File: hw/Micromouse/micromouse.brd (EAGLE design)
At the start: 160 x 100 mm, 23 parts, among them IC1 DSPIC33FJ64MC804-PT, IC2 DRV8833PWR, IC3 LM1117IDTX-5.0_NOPB, IC4 LM1117IDTX-3.3_NOPB, Y1 ECS-200-18-4X-CKM

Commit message: Updated schematic
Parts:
- removed HDR3, HDR4: (no value), SparkFun-Connectors:1X11
- removed IC3: LM1117IDTX-5.0_NOPB, SamacSys_Parts:LM1117IDTX50NOPB
- removed IC4: LM1117IDTX-3.3_NOPB, SamacSys_Parts:LM1117IDTX33NOPB
- removed MOTOR1, MOTOR2: (no value), con-harting:CON06
- removed SENSOR1, SENSOR2, SENSOR3: B3B-ZR(LF)(SN), Headers:B3B-ZR(LF)(SN)
- added C10: 10u, micromouse:0805_POL
- added C11, C12: 100n, micromouse:0805
- added C8: 0.01u, micromouse:0805
- added C9: 2u2, micromouse:0805
- added LED2, LED3, LED4, LED5: (no value), micromouse:LED_3MM
- added M1, M2: (no value), micromouse:JP3Q
- added R1: 0.2, micromouse:0805
- added R10, R2, R4: 10k, micromouse:0805
- added R11, R3, R5: 1k, micromouse:0805
- added R6, R7, R8, R9: 130, micromouse:0805
- added REG1: LM1117-5.0V, micromouse:SOT-223-4
- added REG2: LM1117-3.3V, micromouse:SOT-223-4
- added S1, S3: GP2Y0A51SK0F, micromouse:JP2Y
- added S2: GP2Y0A41SK0F, micromouse:JP2Y
- added SW1, SW2, SW3: B3F-1000, micromouse:B3F-1000
- added T1, T2, T3, T4: NHDTC1X4ETR, micromouse:SOT23
- C1, C2, C3, C4, C5: device micromouse:C0805 -> micromouse:0805_POL
- C6, C7: value C0805C220F5GACTU -> 15p; device SamacSys_Parts:CAPC2012X90N -> micromouse:0805
- HDR1: value (none) -> PICKIT_CON; device SparkFun-Connectors:1X11 -> micromouse:6PIN
- HDR2: value (none) -> UART_CON; device SparkFun-Connectors:1X11 -> micromouse:JP2Y
- Y1: value ECS-200-18-4X-CKM -> (none); device ECS-200-18-4X-CKM:XTAL_ECS-200-18-4X-CKM -> SparkFun-Clocks:HC49US
- moved C7 41.5 mm to (118.1, 55.9)
- moved IC1 36.0 mm to (73.7, 71.1)
- moved C1 35.4 mm to (57.1, 58.4)
- moved HDR1 33.3 mm to (73.7, 31.8)
- moved HDR2 32.1 mm to (45.7, 40.6)
- moved C6 31.0 mm to (111.8, 57.1)
- moved C3 29.8 mm to (90.2, 50.8), turned to 0 degrees
- moved Y1 27.9 mm to (113.0, 48.3), turned to 90 degrees
- moved C2 22.9 mm to (69.8, 36.8)
- moved G1 20.5 mm to (99.1, 49.5)
- moved C4 19.4 mm to (90.2, 44.5), turned to 0 degrees
- moved C5 15.3 mm to (90.2, 39.4), turned to 0 degrees
- moved IC2 1.27 mm to (128.3, 57.1)
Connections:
- net N$1 renamed OSC2
- net N$2 renamed OSC1
- removed net VDD1: IC1.40
- removed net VSS2: IC1.39
- new net LED1: T1.1
- new net LED2: T2.1
- new net LED3: T3.1
- new net LED4: T4.1
- new net M1+: IC2.2, M1.2
- new net M1-: IC2.4, M1.1
- new net M1_CHA: M1.5
- new net M1_CHB: M1.6
- new net M1_IN1: IC2.16
- new net M1_IN2: IC2.15
- new net M2+: IC2.7, M2.2
- new net M2-: IC2.5, M2.1
- new net M2_CHA: M2.5
- new net M2_CHB: M2.6
- new net M2_IN1: IC2.9
- new net M2_IN2: IC2.10
- new net N$10: R7.2, T2.3
- new net N$11: LED3.K, R7.1
- new net N$12: R8.2, T3.3
- new net N$13: LED4.K, R8.1
- new net N$14: R9.2, T4.3
- new net N$15: LED5.K, R9.1
- new net N$16: C11.1, R10.2, R11.1, SW3.4
- new net N$3: C8.2, IC2.11
- new net N$4: C9.1, IC2.14
- new net N$5: IC2.3, IC2.6, R1.1
- new net N$6: C12.1, R4.2, R5.1, SW2.4
- new net N$7: R2.2, R3.1, SW1.4
- new net N$8: R6.2, T1.3
- new net N$9: LED2.K, R6.1
- new net PGC: HDR1.4
- new net PGD: HDR1.5
- new net S1_OUT: S1.1
- new net S2_OUT: S2.3
- new net S3_OUT: S3.1
- new net SW1: R5.2
- new net SW2: R11.2
- new net UART_RX: HDR2.2
- new net UART_TX: HDR2.1
- net +3V3: now also HDR1.2, IC1.40, IC2.1, IC2.8, M1.4, M2.4, R10.1, R2.1, R4.1, REG2.2, REG2.4; no longer IC4.2
- net +5V: now also LED2.A, LED3.A, LED4.A, LED5.A, REG1.2, REG1.4, REG2.3, S1.3, S2.1, S3.3; no longer IC3.4, IC4.3
- net +9V: now also C10.1, C8.1, IC2.12, REG1.3; no longer IC3.3
- net GND: now also C10.2, C11.2, C12.2, C9.2, HDR1.3, HDR2.3, IC1.39, M1.3, M2.3, R1.2, REG1.1, REG2.1, S1.2, S2.2, S3.2, SW1.2, SW2.2, SW3.2, T1.2, T2.2, T3.2, T4.2; no longer IC3.1, IC4.1
- net MCLR: now also HDR1.1, R3.2

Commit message: Updated EAGLE project
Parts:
- removed S1, S3: GP2Y0A51SK0F, micromouse:JP2Y
- removed S2: GP2Y0A41SK0F, micromouse:JP2Y
- added J1, J2: GP2Y0A51SK0F, micromouse:B3B-ZR(LF)(SN)
- added J3: GP2Y0A41SK0F, micromouse:B3B-PH-K-S
- added R12: 0.2, micromouse:0805
- moved C8 152.7 mm to (-4.45, -1.27)
- moved C9 150.4 mm to (-0.64, -1.91), turned to 270 degrees
- moved C10 144.2 mm to (-7.62, -1.27), turned to 90 degrees
- moved IC2 141.5 mm to (-3.81, 6.35), turned to 270 degrees
- moved R1 134.3 mm to (0.64, 8.89), turned to 270 degrees
- moved C6 127.7 mm to (-11.5, 23.6), turned to 180 degrees
- moved M2 126.5 mm to (-21.6, 17.1)
- moved C7 126.1 mm to (-3.76, 23.6)
- moved M1 123.2 mm to (-5.71, 17.1)
- moved Y1 122.5 mm to (-7.62, 27.3), turned to 180 degrees
- moved HDR1 108.7 mm to (-3.81, -44.5)
- moved HDR2 91.1 mm to (0.00, -38.1), turned to 180 degrees
- moved IC1 88.6 mm to (-8.26, 37.5), turned to 270 degrees
- moved C3 87.3 mm to (3.17, 43.8), turned to 180 degrees
- moved R7 82.8 mm to (-22.9, 37.5), turned to 90 degrees
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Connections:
- new net N$1: IC2.6, R12.1
- net +5V: now also J1.1, J2.1, J3.3; no longer S1.3, S2.1, S3.3
- net GND: now also J1.2, J2.2, J3.2, R12.2; no longer S1.2, S2.2, S3.2
- net N$5: no longer IC2.6
- net S1_OUT: now also J1.3; no longer S1.1
- net S2_OUT: now also J3.1; no longer S2.3
- net S3_OUT: now also J2.3; no longer S3.1
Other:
- board size 160 x 100 mm -> 60 x 112 mm

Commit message: First routing on PCB
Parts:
- removed R10: 10k, micromouse:0805
- removed R11: 1k, micromouse:0805
- removed SW2, SW3: B3F-1000, micromouse:B3F-1000
- added C13, C14: (no value), micromouse:0805
- added SW_RST: B3F-1000, micromouse:B3F-1000
- C11: value 100n -> (none)
- moved HDR1 82.8 mm to (-27.9, 34.8), turned to 270 degrees
- moved HDR2 80.7 mm to (12.0, 41.7)
- moved R4 68.7 mm to (-0.11, -37.1)
- moved SW1 66.0 mm to (0.09, -29.4), turned to 0 degrees
- moved R5 63.6 mm to (3.23, -35.3), turned to 270 degrees
- moved C12 61.0 mm to (-0.12, -34.2), turned to 180 degrees
- moved LED3 49.1 mm to (-4.10, -5.82)
- moved R7 49.1 mm to (0.34, -5.82)
- moved T2 49.1 mm to (3.52, -5.82)
- moved LED2 49.1 mm to (-4.10, 0.53)
- moved LED4 49.1 mm to (-4.10, -12.2)
- moved LED5 49.1 mm to (-4.10, -18.5)
- moved R6 49.1 mm to (0.34, 0.53)
- moved R8 49.1 mm to (0.34, -12.2)
- moved R9 49.1 mm to (0.34, -18.5)
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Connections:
- removed net N$16: C11.1, R10.2, R11.1, SW3.4
- removed net PGC: HDR1.4
- removed net PGD: HDR1.5
- removed net PGEC1: IC1.22
- removed net PGED1: IC1.21
- removed net SW2: R11.2
- net +3V3: now also C11.1, C13.2, C14.2; no longer R10.1
- net GND: now also C13.1, C14.1, SW_RST.2; no longer SW2.2, SW3.2
- net M1_CHA: now also IC1.36, M1.6; no longer M1.5
- net M1_CHB: now also IC1.37, M1.5; no longer M1.6
- net M1_IN1: now also IC1.1
- net M1_IN2: now also IC1.2
- net M2_CHA: now also IC1.43, M2.6; no longer M2.5
- net M2_CHB: now also IC1.44, M2.5; no longer M2.6
- net M2_IN1: now also IC1.4
- net M2_IN2: now also IC1.3
- net N$6: now also SW1.4; no longer SW2.4
- net N$7: now also SW_RST.4; no longer SW1.4
- net PGEC3: now also HDR1.5
- net PGED3: now also HDR1.4
- net S1_OUT: now also IC1.20
- net S2_OUT: now also IC1.21
- net S3_OUT: now also IC1.22
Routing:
- net +3V3: track 0.00 -> 158.0 mm, vias 0 -> 3
- net +5V: track 0.00 -> 79.0 mm
- net M1+: track 0.00 -> 65.5 mm, vias 0 -> 1
- net M1-: track 0.00 -> 59.6 mm, vias 0 -> 1
- net +9V: track 0.00 -> 54.1 mm
- net M2-: track 0.00 -> 41.6 mm, vias 0 -> 1
- net M2+: track 0.00 -> 39.7 mm, vias 0 -> 1
- net MCLR: track 0.00 -> 35.1 mm
- net PGEC3: track 0.00 -> 28.4 mm, vias 0 -> 1
- net PGED3: track 0.00 -> 27.3 mm, vias 0 -> 1
- net S1_OUT: track 0.00 -> 22.0 mm
- net M1_CHB: track 0.00 -> 19.8 mm
- net M1_CHA: track 0.00 -> 17.6 mm
- net S2_OUT: track 0.00 -> 16.8 mm
- net M2_CHB: track 0.00 -> 13.1 mm
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
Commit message: Cleanup on PCB routing
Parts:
- moved C2 4.40 mm to (28.3, 17.9), turned to 270 degrees
- moved G1 3.16 mm to (20.1, 14.9)
- moved REG1 3.06 mm to (25.9, 24.8)
- moved C3 2.83 mm to (22.6, 29.4)
- moved C5 2.80 mm to (25.7, 42.6)
- moved REG2 2.80 mm to (24.7, 36.9)
- moved HDR2 2.72 mm to (13.6, 39.5)
- moved C6 2.15 mm to (-18.8, 30.8), turned to 90 degrees
- moved C7 1.31 mm to (-18.8, 35.8), turned to 90 degrees
- moved C1 0.72 mm to (1.94, 36.4)
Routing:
- net +9V: track 54.1 -> 66.9 mm
- net N$7: track 0.28 -> 7.00 mm
- net +5V: track 79.0 -> 74.3 mm
- net +3V3: track 158.0 -> 161.8 mm
- net N$1: track 8.52 -> 7.70 mm
- net VCAP/VDDCORE: track 3.02 -> 2.25 mm

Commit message: Updated PCB
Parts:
- moved LED5 15.0 mm to (-5.30, -33.5)
- moved R9 15.0 mm to (-0.85, -33.5)
- moved T4 15.0 mm to (2.32, -33.5)
- moved LED4 15.0 mm to (-5.30, -27.2)
- moved R8 15.0 mm to (-0.85, -27.2)
- moved T3 15.0 mm to (2.32, -27.2)
- moved LED2 15.0 mm to (-5.30, -14.5)
- moved LED3 15.0 mm to (-5.30, -20.8)
- moved R6 15.0 mm to (-0.85, -14.5)
- moved R7 15.0 mm to (-0.85, -20.8)
- moved T1 15.0 mm to (2.32, -14.5)
- moved T2 15.0 mm to (2.32, -20.8)
- moved G1 14.9 mm to (5.33, 16.9), turned to 180 degrees
- moved R5 13.9 mm to (-6.47, -45.2), turned to 180 degrees
- moved SW1 12.7 mm to (-0.64, -42.1), turned to 270 degrees
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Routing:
- net +5V: track 74.3 -> 155.6 mm, vias 0 -> 1
- net +3V3: track 161.8 -> 228.7 mm
- net M2+: track 39.7 -> 55.0 mm
- net +9V: track 66.9 -> 81.4 mm
- net GND: track 0.00 -> 9.08 mm, vias 0 -> 11
- net M2-: track 41.6 -> 49.0 mm
- net M1-: track 59.6 -> 64.7 mm
- net M1+: track 65.5 -> 70.3 mm
- net N$9: track 0.00 -> 3.57 mm
- net N$13: track 0.00 -> 3.57 mm
- net N$11: track 0.00 -> 3.57 mm
- net N$15: track 0.00 -> 3.57 mm
- net N$14: track 0.00 -> 2.47 mm
- net N$12: track 0.00 -> 2.47 mm
- net N$8: track 0.00 -> 2.47 mm
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
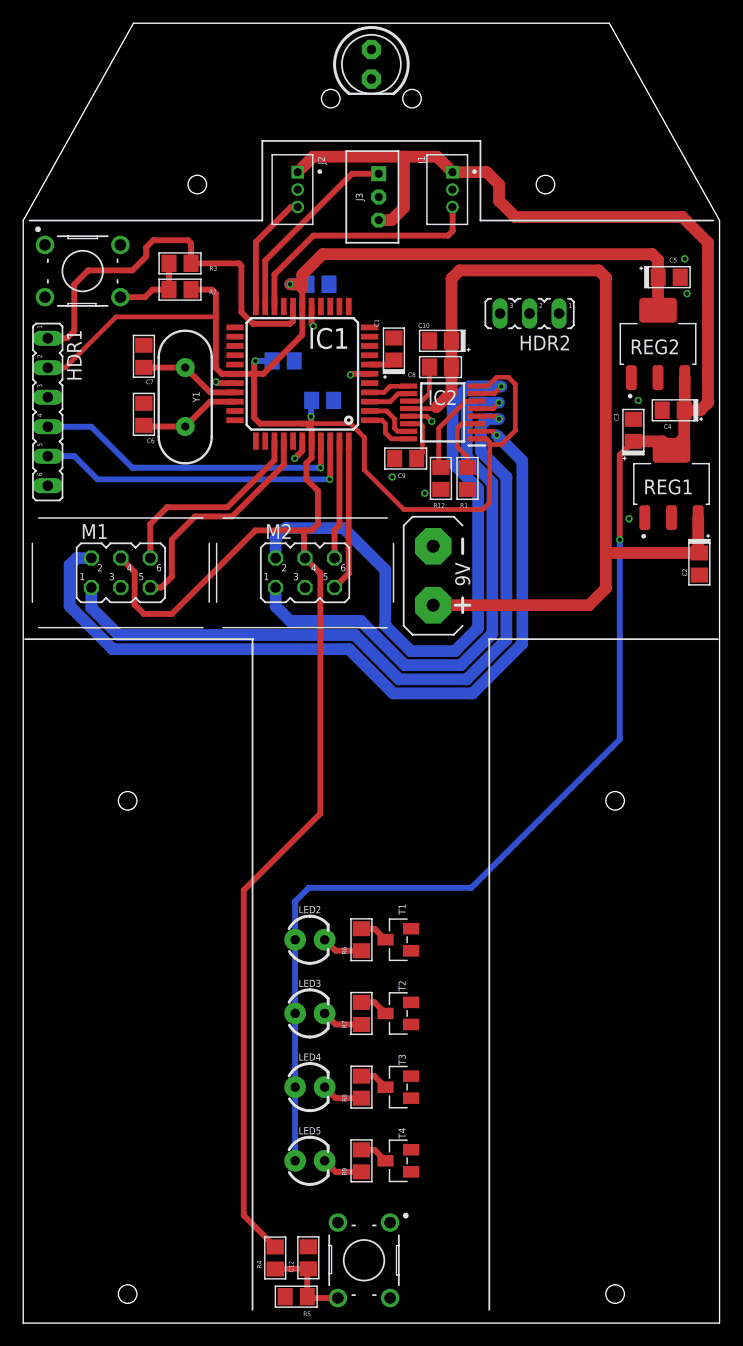
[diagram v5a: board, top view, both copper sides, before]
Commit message: Added Bluetooth module
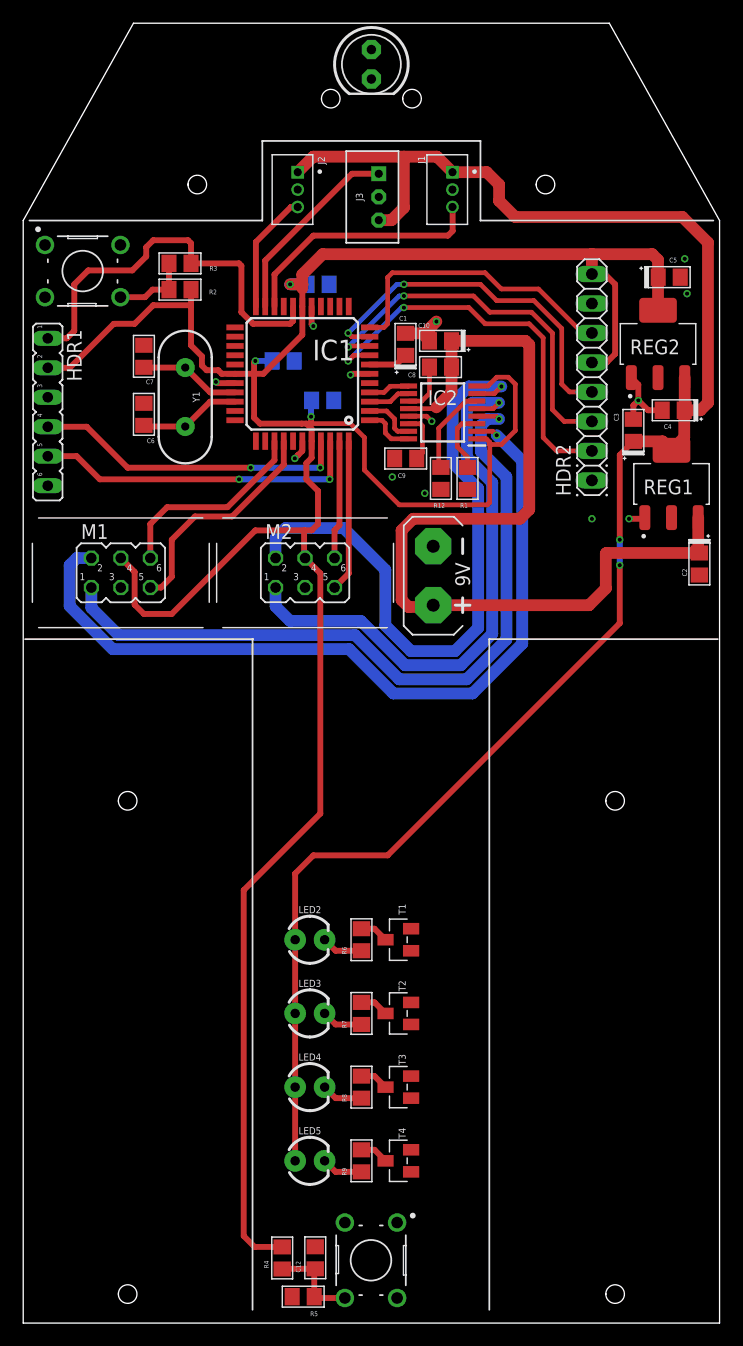
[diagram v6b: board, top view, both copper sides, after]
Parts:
- HDR2: value UART_CON -> BLUETOOTH; device micromouse:JP2Y -> micromouse:1X08
- moved HDR2 7.68 mm to (19.0, 34.0), turned to 90 degrees
- moved C1 1.08 mm to (2.94, 36.8)
- moved R4 0.60 mm to (-7.68, -41.9)
- moved SW1 0.60 mm to (-0.04, -42.1)
- moved C12 0.60 mm to (-4.83, -41.9)
- moved R5 0.60 mm to (-5.88, -45.2)
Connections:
- removed net PGEC2: IC1.9
- removed net PGED2: IC1.8
- new net BT_CTS: HDR2.2, IC1.8
- new net BT_MOD: HDR2.1
- new net BT_RTS: HDR2.6, IC1.11
- net +3V3: now also HDR2.5, HDR2.8
- net GND: now also HDR2.7; no longer HDR2.3
- net UART_RX: now also HDR2.3, IC1.9; no longer HDR2.2
- net UART_TX: now also HDR2.4, IC1.10; no longer HDR2.1
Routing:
- net BT_CTS: track 0.00 -> 35.1 mm, vias 0 -> 2
- net UART_RX: track 0.00 -> 33.1 mm, vias 0 -> 2
- net UART_TX: track 0.00 -> 31.4 mm, vias 0 -> 2
- net BT_RTS: track 0.00 -> 25.6 mm
- net GND: track 9.08 -> 21.2 mm, vias 11 -> 13
- net +3V3: track 228.7 -> 240.2 mm
- net +5V: track 155.6 -> 151.1 mm, vias 1 -> 2
- net +9V: track 81.4 -> 80.2 mm
- net VCAP/VDDCORE: track 2.25 -> 3.42 mm
- net PGED3: vias 1 -> 2
- net PGEC3: vias 1 -> 2
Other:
- outline, holes or cut-outs redrawn

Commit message: Updated PCB
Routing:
- net +5V: track 151.1 -> 156.9 mm
- net +3V3: track 240.2 -> 241.0 mm
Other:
- outline, holes or cut-outs redrawn

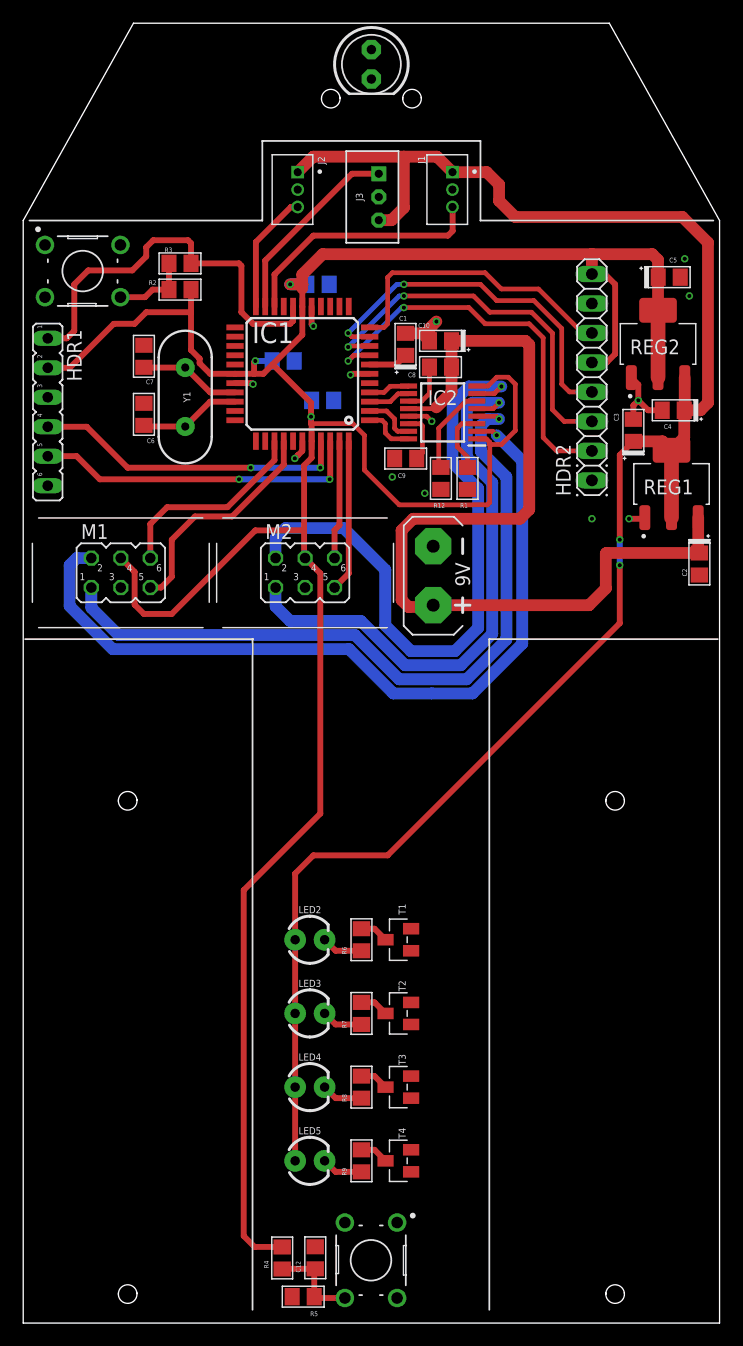
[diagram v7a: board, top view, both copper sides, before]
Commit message: Tighter layout for PCB; Removed transistors for LEDs
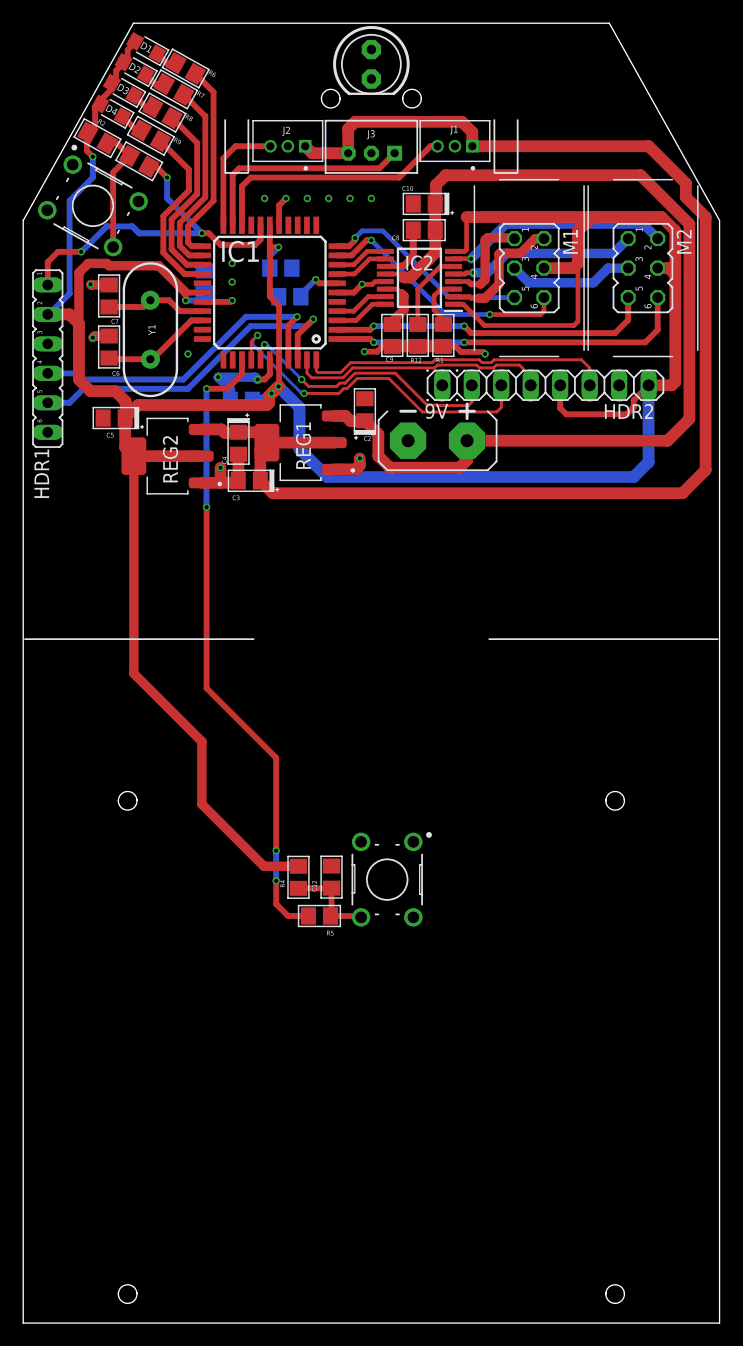
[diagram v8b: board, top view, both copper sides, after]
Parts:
- removed LED2, LED3, LED4, LED5: (no value), micromouse:LED_3MM
- removed T1, T2, T3, T4: NHDTC1X4ETR, micromouse:SOT23
- added D1, D2, D3, D4: LED_0805, micromouse:SMD_LED_0805
- moved R9 90.2 mm to (-19.0, 54.8), turned to 330.8 degrees
- moved R8 85.7 mm to (-18.0, 56.8), turned to 330.8 degrees
- moved R7 81.2 mm to (-17.0, 58.8), turned to 330.8 degrees
- moved R6 76.6 mm to (-16.0, 60.6), turned to 330.8 degrees
- moved C5 49.3 mm to (-22.2, 30.5), turned to 180 degrees
- moved M1 43.9 mm to (13.6, 43.4), turned to 270 degrees
- moved REG2 43.4 mm to (-17.6, 27.2), turned to 90 degrees
- moved M2 39.2 mm to (23.4, 43.4), turned to 270 degrees
- moved C4 37.6 mm to (-11.4, 28.3), turned to 270 degrees
- moved C3 33.4 mm to (-10.5, 25.1), turned to 180 degrees
- moved SW1 32.8 mm to (1.36, -9.29)
- moved C12 32.8 mm to (-3.44, -9.07)
- moved R4 32.8 mm to (-6.29, -9.09)
- moved R5 32.8 mm to (-4.47, -12.4)
- moved REG1 32.2 mm to (-6.10, 28.4), turned to 90 degrees
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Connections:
- removed net N$10: R7.2, T2.3
- removed net N$11: LED3.K, R7.1
- removed net N$12: R8.2, T3.3
- removed net N$14: R9.2, T4.3
- removed net N$8: R6.2, T1.3
- new net N$2: D2.P$1, R7.1
- net +3V3: now also D1.P$2, D2.P$2, D3.P$2, D4.P$2
- net +5V: no longer LED2.A, LED3.A, LED4.A, LED5.A
- net BT_CTS: now also IC1.38; no longer IC1.8
- net BT_RTS: now also IC1.44; no longer IC1.11
- net GND: no longer T1.2, T2.2, T3.2, T4.2
- net LED1: now also IC1.23, R6.2; no longer T1.1
- net LED2: now also IC1.24, R7.2; no longer T2.1
- net LED3: now also IC1.25, R8.2; no longer T3.1
- net LED4: now also IC1.26, R9.2; no longer T4.1
- net M1_CHA: now also IC1.10; no longer IC1.36
- net M1_CHB: now also IC1.11; no longer IC1.37
- net M1_IN1: now also IC1.3; no longer IC1.1
- net M1_IN2: now also IC1.4; no longer IC1.2
- net M2_CHA: now also IC1.1; no longer IC1.43
- net M2_CHB: now also IC1.2; no longer IC1.44
- net M2_IN1: now also IC1.9; no longer IC1.4
- net M2_IN2: now also IC1.8; no longer IC1.3
- net N$13: now also D3.P$1; no longer LED4.K
- net N$15: now also D4.P$1; no longer LED5.K
- net N$9: now also D1.P$1; no longer LED2.K
- net SW1: now also IC1.36
- net UART_RX: now also IC1.37; no longer IC1.9
- net UART_TX: now also IC1.43; no longer IC1.10
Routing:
- net M1+: track 70.3 -> 11.5 mm, vias 1 -> 0
- net M1-: track 64.7 -> 9.02 mm, vias 1 -> 0
- net SW1: track 0.00 -> 54.9 mm, vias 0 -> 4
- net +5V: track 156.9 -> 118.8 mm, vias 2 -> 0
- net M2+: track 55.0 -> 19.4 mm
- net M2-: track 49.0 -> 16.3 mm
- net GND: track 21.0 -> 52.7 mm, vias 13 -> 19
- net +3V3: track 241.0 -> 267.4 mm, vias 3 -> 5
- net M2_CHA: track 10.3 -> 31.0 mm, vias 0 -> 2
- net LED1: track 0.00 -> 17.5 mm
- net LED2: track 0.00 -> 17.0 mm
- net LED3: track 0.00 -> 16.3 mm
- net LED4: track 0.00 -> 15.7 mm
- net M2_CHB: track 13.1 -> 27.9 mm, vias 0 -> 2
- net BT_CTS: track 35.1 -> 24.0 mm
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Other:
- outline, holes or cut-outs redrawn
